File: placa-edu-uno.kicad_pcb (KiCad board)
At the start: 2 copper layers, 97.1 x 58.9 mm, 70 parts, among them J1 Conn_02x20_Odd_Even_MountingP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, J10 HEADER, J11 HEADER, J12 HEADER, J13 HEADER, J14 HEADER, J15 HEADER, J2 Screw_Terminal_01x02, J3 Screw_Terminal_01x02, J4 Screw_Terminal_01x02, J5 Screw_Terminal_01x02, J6 Conn_02x13_Odd_Even, J7 HEADER, J8 HEADER, J9 HEADER, U1 PCA9685PW_118, U2 MAX98357AETE_T, U3 MAX98357AETE_T, U4 ICS-43434, U5 ICS-43434, U6 LM73605

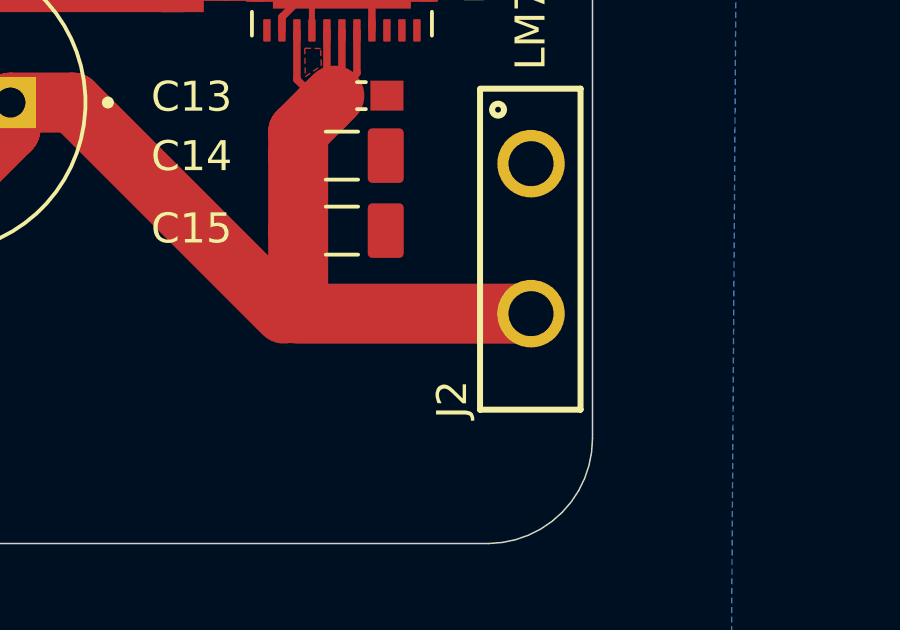
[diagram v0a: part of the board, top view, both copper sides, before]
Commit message: Se agregó símbolo de polaridad a J2 en la serigrafía
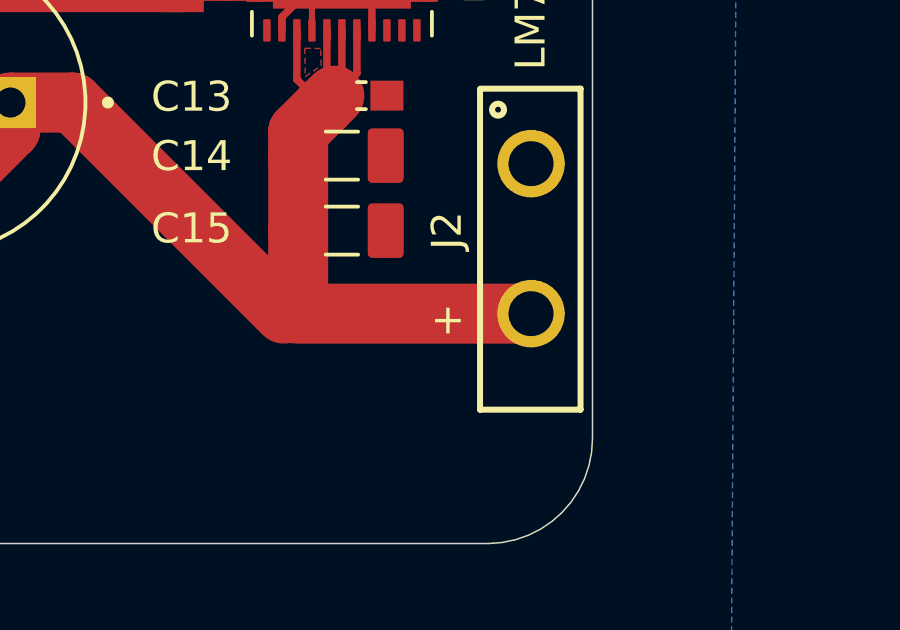
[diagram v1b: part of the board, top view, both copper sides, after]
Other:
- board text added: "+"
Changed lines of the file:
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@@
 		(at 82.804 46.268 -90)
 		(property "Reference" "J2"
-			(at 5.357 2.629 90)
+			(at -0.268 2.804 90)
 			(layer "F.SilkS")
 			(effects
@@
 		(layer "Edge.Cuts")
 	)
+	(gr_text "+"
+		(at 80 49 90)
+		(layer "F.SilkS")
+		(effects
+			(font
+				(size 1 1)
+				(thickness 0.16)
+			)
+		)
+	)
 	(dimension

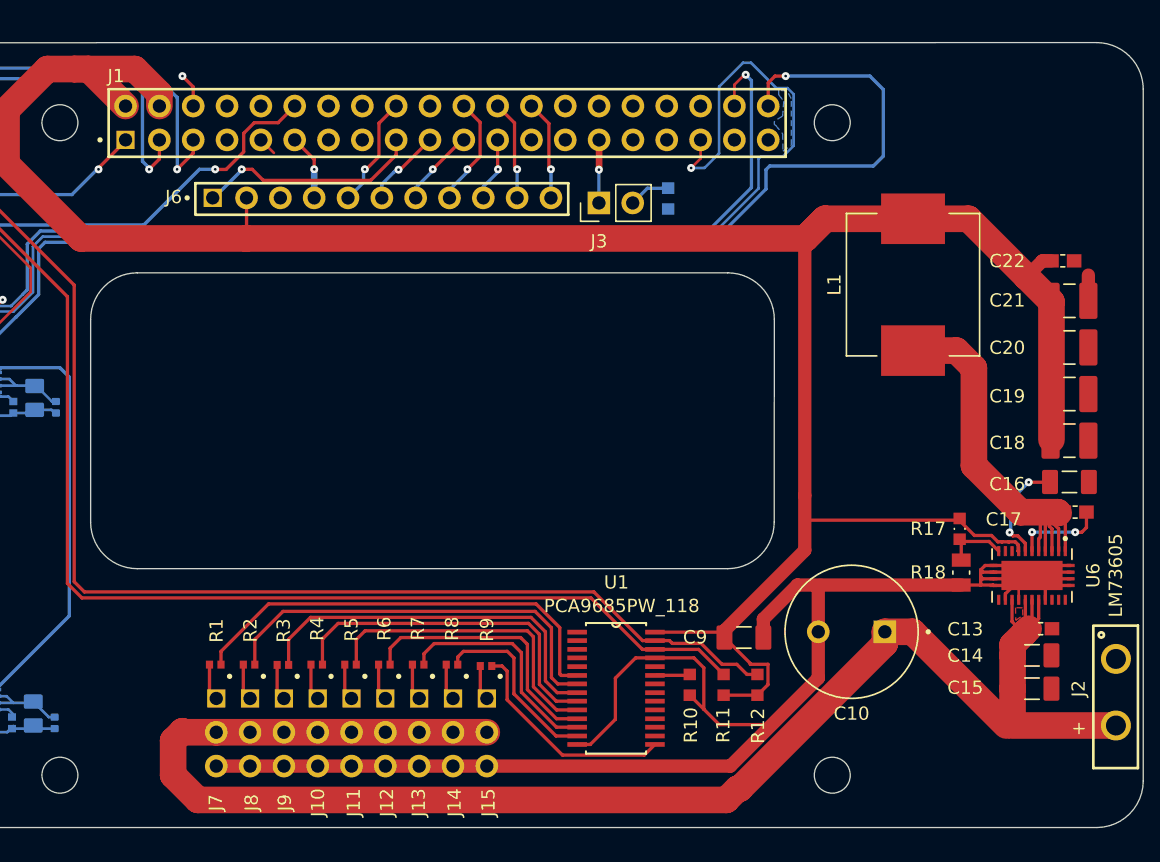
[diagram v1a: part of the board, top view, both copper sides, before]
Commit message: Se añadió serigrafía con nombres, logos y pines de los servos
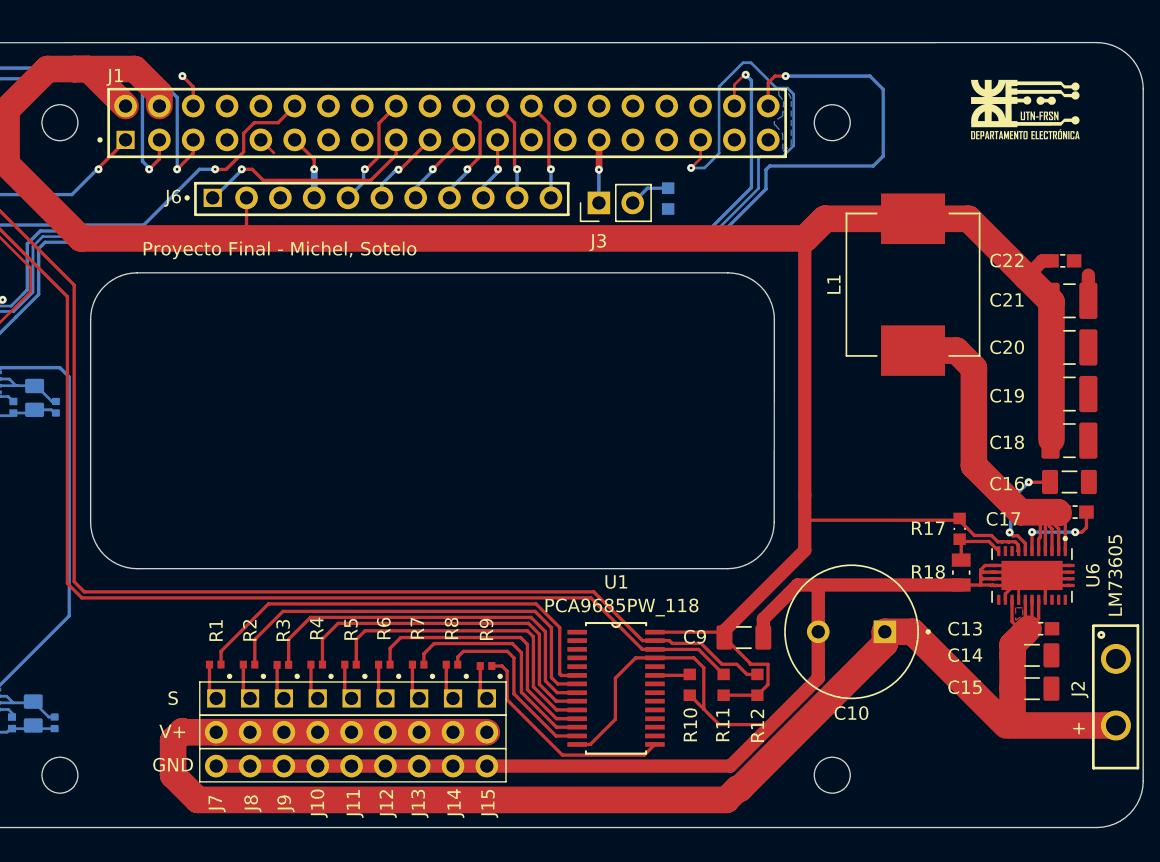
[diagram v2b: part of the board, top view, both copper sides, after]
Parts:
- added G***: LOGO, Footprints:logo_utn, F.Cu at (76.0, 2.50)
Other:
- board text added: "GND"
- board text added: "Proyecto Final - Michel, Sotelo"
- board text added: "S"
- board text added: "V+"

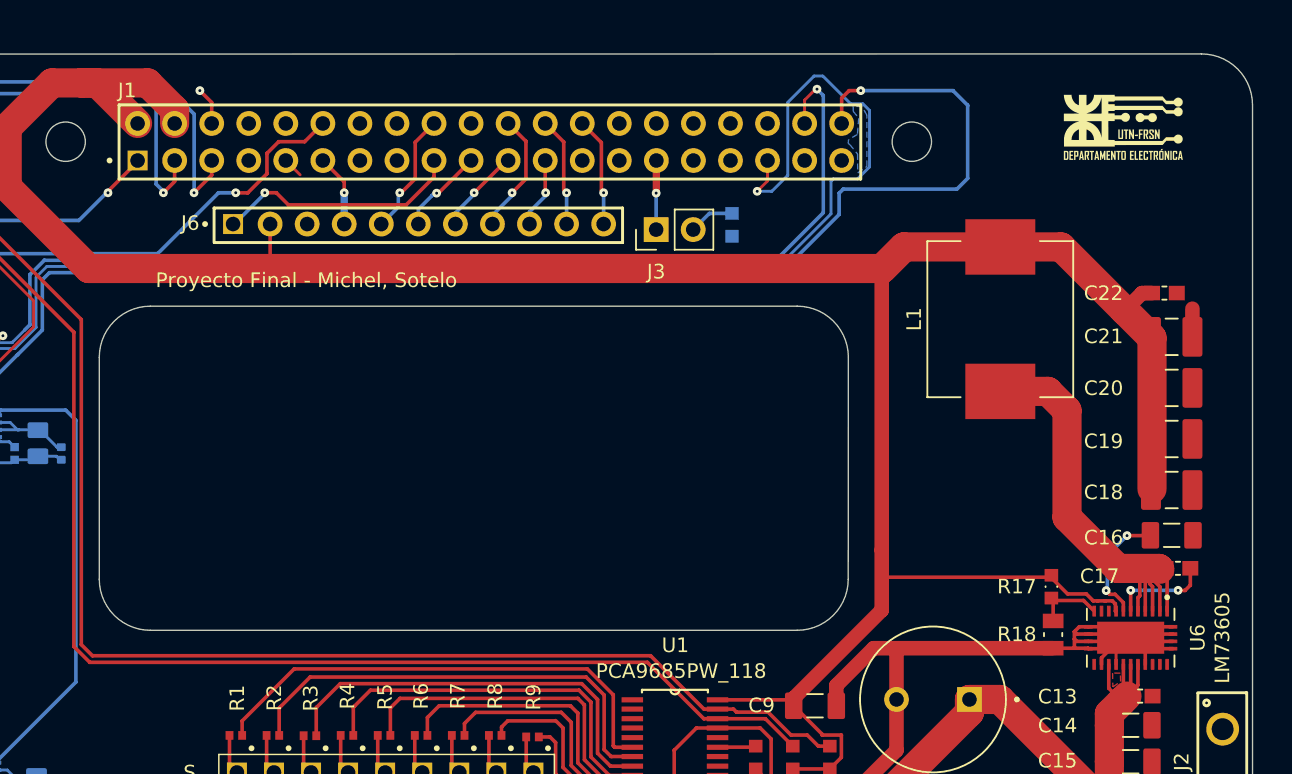
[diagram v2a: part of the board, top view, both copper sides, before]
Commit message: Se corrigio la posicion de la serigrafia en J4 y J5, y el nombre de la U1 PCA9685
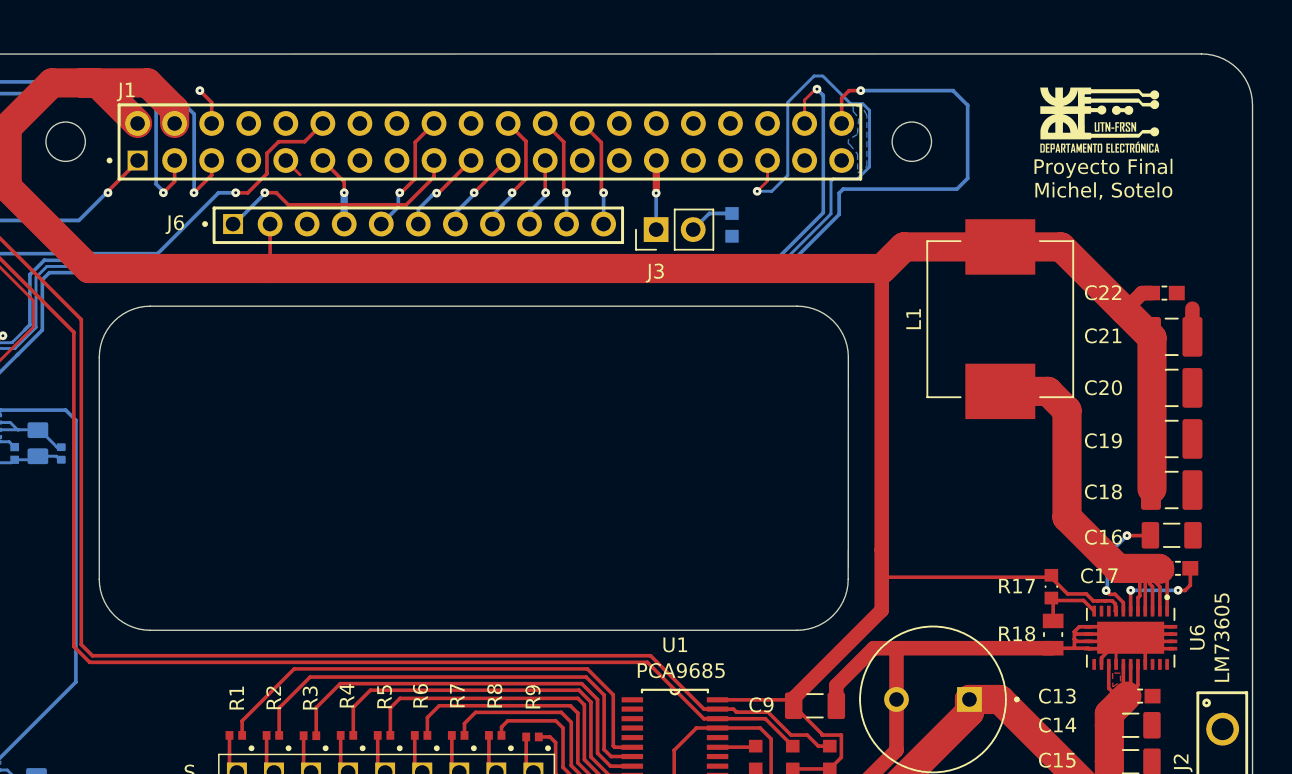
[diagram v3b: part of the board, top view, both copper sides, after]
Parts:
- U1: value PCA9685PW_118 -> PCA9685
- moved G*** 1.69 mm to (74.4, 2.00)
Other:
- board text added: "Proyecto Final Michel, Sotelo"
- board text removed: "Proyecto Final - Michel, Sotelo"
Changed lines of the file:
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@@
 		(at 14.97464 9.144)
 		(property "Reference" "J6"
-			(at -2.93464 -0.064 0)
+			(at -3.91464 -0.054 0)
 			(layer "F.SilkS")
 			(effects
@@
 	(footprint "Footprints:logo_utn"
 		(layer "F.Cu")
-		(at 76 2.5)
+		(at 74.382936 2.002394)
 		(property "Reference" "G***"
 			(at 7.5 -1 0)
@@
 			)
 		)
-		(property "Value" "PCA9685PW_118"
+		(property "Value" "PCA9685"
 			(at 0.4272 -6.184 0)
 			(layer "F.SilkS")
@@
 		(at -10.01 41.78)
 		(property "Reference" "J5"
-			(at 0 0.5 180)
+			(at 0 0.5 0)
 			(unlocked yes)
 			(layer "B.SilkS")
@@
 		(at -9.95 17.13)
 		(property "Reference" "J4"
-			(at 0 0.5 180)
+			(at 0 0.5 0)
 			(unlocked yes)
 			(layer "B.SilkS")
@@
 		)
 	)
-	(gr_text "Proyecto Final - Michel, Sotelo"
-		(at 20 13 0)
+	(gr_text "Proyecto Final\nMichel, Sotelo"
+		(at 74.632936 6.052394 0)
 		(layer "F.SilkS")
 		(effects
@@
 		)
 	)
+	(gr_text "+"
+		(at -10.05 25.12 90)
+		(layer "B.SilkS")
+		(effects
+			(font
+				(size 1 1)
+				(thickness 0.16)
+			)
+		)
+	)
+	(gr_text "+"
+		(at -10.05 49.66 90)
+		(layer "B.SilkS")
+		(effects
+			(font
+				(size 1 1)
+				(thickness 0.125)
+			)
+		)
+	)
 	(dimension
 		(type aligned)
@@
 	)
 	(group ""
+		(members "24964b83-0313-41aa-acba-c239b679768d" "a6e9302c-9ada-484b-ab14-5500d311d555")
+	)
+	(group ""

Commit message: Mejora de ruteo
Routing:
- net GND: track 183.8 -> 145.2 mm
- net 5V_Fuente: track 124.3 -> 103.1 mm
- net GPIO_19_FS_PCM: track 139.0 -> 121.1 mm
- net GPIO_18_CLK_PCM: track 92.6 -> 94.3 mm
- net 3.3V_RPI: track 125.5 -> 126.6 mm
- net GPIO_20_DIN_PCM: track 114.9 -> 115.5 mm
- net GPIO_21_DOUT_PCM: track 125.5 -> 126.1 mm
- net /Amplificadores/OUT_N2: track 4.89 -> 5.43 mm
- added copper zone on F.Cu, net 5V_Fuente

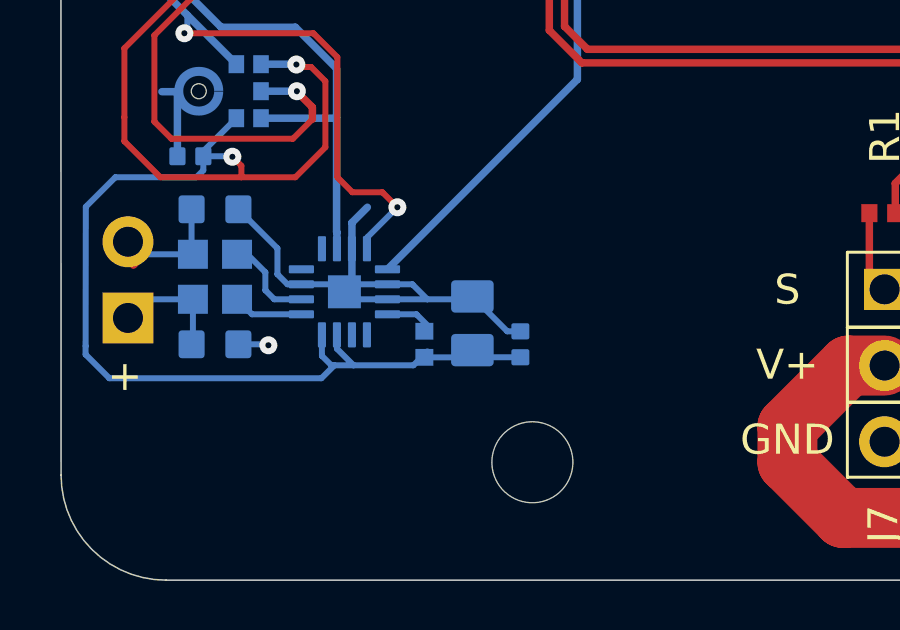
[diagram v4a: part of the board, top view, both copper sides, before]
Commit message: Se movio la posicion de c y r en el amplificador de abajo para que no quede sobre el borde del mounting hole.
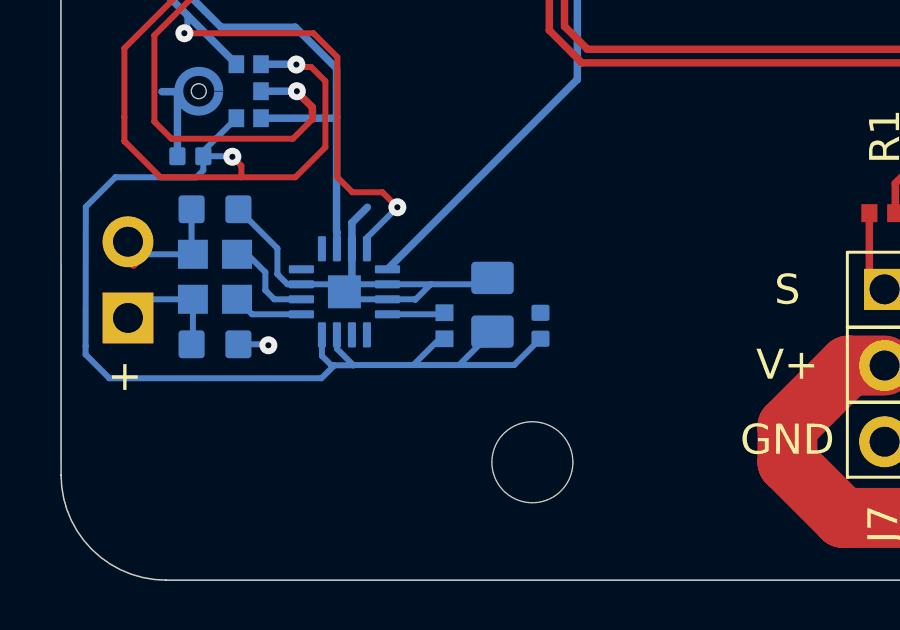
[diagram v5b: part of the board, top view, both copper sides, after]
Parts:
- moved C6 0.91 mm to (2.17, 47.2)
- moved C5 0.91 mm to (3.77, 48.0)
- moved R14 0.91 mm to (0.57, 48.0)
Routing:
- net 3.3V_RPI: track 126.6 -> 130.1 mm
- net GND: track 145.2 -> 143.8 mm
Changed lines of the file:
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@@
 	(footprint "CL21A106KOQNNNE:CAPC2012X140N"
 		(layer "B.Cu")
-		(at 1.5 47.868 90)
+		(at 2.17 47.25 90)
 		(property "Reference" "C6"
 			(at 2.748 0.33 90)
@@
 	(footprint "0402WGF6803TCE:RESC1005X40N"
 		(layer "B.Cu")
-		(at -0.1 48.568 90)
+		(at 0.57 47.95 90)
 		(property "Reference" "R14"
-			(at -2.482 0.12 270)
+			(at 2.99 -0.01 270)
 			(layer "B.SilkS")
 			(effects
@@
 	(footprint "CL05B104KO5NNNC:CAPC1005X55N"
 		(layer "B.Cu")
-		(at 3.1 48.568 90)
+		(at 3.77 47.95 90)
 		(property "Reference" "C5"
 			(at 2.028 0.18 90)
@@
 	)
 	(segment
-		(start 1.405 47.068)
-		(end 1.5 46.973)
-		(width 0.2)
-		(layer "B.Cu")
-		(net 1)
-	)
-	(segment
 		(start -4.2 46.568)
 		(end -3.015 46.568)
@@
 	)
 	(segment
-		(start -0.5 46.568)
-		(end 0 47.068)
+		(start -2.963745 22.747745)
+		(end -2.713745 22.997745)
 		(width 0.2)
 		(layer "B.Cu")
@@
 	)
 	(segment
-		(start -2.963745 22.747745)
-		(end -2.713745 22.997745)
+		(start -1.33 46.568)
+		(end 0.12 46.568)
 		(width 0.2)
 		(layer "B.Cu")
@@
 	)
 	(segment
-		(start 2.663 48.136)
-		(end 1.5 46.973)
-		(width 0.2)
-		(layer "B.Cu")
-		(net 1)
-	)
-	(segment
 		(start -2.515 46.568)
 		(end -2.765 46.818)
@@
 	)
 	(segment
-		(start 1.5 46.973)
-		(end 1.373 47.1)
-		(width 0.2)
-		(layer "B.Cu")
-		(net 1)
-	)
-	(segment
 		(start 60.45 38.36831)
 		(end 60.6 38.21831)
@@
 	)
 	(segment
-		(start 0 47.068)
-		(end 1.405 47.068)
-		(width 0.2)
-		(layer "B.Cu")
-		(net 1)
-	)
-	(segment
-		(start -1.33 47.068)
-		(end 0 47.068)
-		(width 0.2)
-		(layer "B.Cu")
-		(net 1)
-	)
-	(segment
 		(start -8.332 42.3)
 		(end -8.332 40.1895)
@@
 	)
 	(segment
-		(start 3.1 48.136)
-		(end 2.663 48.136)
+		(start 1.957 46.568)
+		(end 2.17 46.355)
+		(width 0.2)
+		(layer "B.Cu")
+		(net 1)
+	)
+	(segment
+		(start 0.112 46.568)
+		(end 0.12 46.568)
 		(width 0.2)
 		(layer "B.Cu")
@@
 	)
 	(segment
-		(start -1.33 46.568)
-		(end -0.5 46.568)
-		(width 0.2)
-		(layer "B.Cu")
-		(net 1)
-	)
-	(segment
 		(start -1.278745 22.747745)
 		(end -0.3 22.747745)
@@
 	)
 	(segment
+		(start -0.4 47.08)
+		(end 0.112 46.568)
+		(width 0.2)
+		(layer "B.Cu")
+		(net 1)
+	)
+	(segment
 		(start -8.332 40.1895)
 		(end -8.29 40.1475)
@@
 	)
 	(segment
+		(start 0.12 46.568)
+		(end 1.957 46.568)
+		(width 0.2)
+		(layer "B.Cu")
+		(net 1)
+	)
+	(segment
 		(start -6.217866 19.317866)
 		(end -6.2 19.3)
@@
 	)
 	(segment
+		(start -1.33 47.068)
+		(end -0.412 47.068)
+		(width 0.2)
+		(layer "B.Cu")
+		(net 1)
+	)
+	(segment
 		(start -5.1 20.336)
 		(end -6.217866 20.336)
@@
 	)
 	(segment
+		(start -0.412 47.068)
+		(end -0.4 47.08)
+		(width 0.2)
+		(layer "B.Cu")
+		(net 1)
+	)
+	(segment
 		(start -6.3 48.568)
 		(end -5.332 48.568)
@@
 	)
 	(segment
-		(start -0.1 49.003)
-		(end 1.26 49.003)
-		(width 0.2)
-		(layer "B.Cu")
-		(net 2)
-	)
-	(segment
 		(start -10.6 49.7)
 		(end -3.532 49.7)
@@
 	)
 	(segment
-		(start -0.465 49.268)
-		(end 0 48.803)
-		(width 0.2)
-		(layer "B.Cu")
-		(net 2)
-	)
-	(segment
 		(start -2.5 25.504)
 		(end -3.1 25.504)
@@
 	(segment
 		(start -2.461842 49.268)
-		(end -0.465 49.268)
-		(width 0.2)
-		(layer "B.Cu")
-		(net 2)
-	)
-	(segment
-		(start 1.26 49.003)
-		(end 1.5 48.763)
+		(end -2.453842 49.26)
 		(width 0.2)
 		(layer "B.Cu")
@@
 	)
 	(segment
-		(start 3.1 49)
-		(end 1.737 49)
+		(start 1.055 49.26)
+		(end 2.13745 48.17755)
+		(width 0.2)
+		(layer "B.Cu")
+		(net 2)
+	)
+	(segment
+		(start -2.453842 49.26)
+		(end -0.473 49.26)
 		(width 0.2)
 		(layer "B.Cu")
@@
 	)
 	(segment
+		(start 0.4065 48.385)
+		(end 0.57 48.385)
+		(width 0.2)
+		(layer "B.Cu")
+		(net 2)
+	)
+	(segment
 		(start -4.376884 39.232)
 		(end -4.366942 39.241942)
@@
 	)
 	(segment
-		(start 1.737 49)
-		(end 1.5 48.763)
-		(width 0.2)
-		(layer "B.Cu")
-		(net 2)
-	)
-	(segment
 		(start -2.5 25.504)
 		(end -0.201 25.504)
@@
 	)
 	(segment
+		(start -0.465 49.2565)
+		(end 0.4065 48.385)
+		(width 0.2)
+		(layer "B.Cu")
+		(net 2)
+	)
+	(segment
 		(start -3.532 49.7)
 		(end -3.1 49.268)
@@
 	)
 	(segment
+		(start 2.892 49.26)
+		(end 3.77 48.382)
+		(width 0.2)
+		(layer "B.Cu")
+		(net 2)
+	)
+	(segment
 		(start -7.468 42.3)
 		(end -6.51645 42.3)
@@
 	)
 	(segment
+		(start 1.055 49.26)
+		(end 2.892 49.26)
+		(width 0.2)
+		(layer "B.Cu")
+		(net 2)
+	)
+	(segment
 		(start 1.6 25.063)
 		(end 2.865416 25.063)
@@
 	)
 	(segment
+		(start -0.473 49.26)
+		(end 1.055 49.26)
+		(width 0.2)
+		(layer "B.Cu")
+		(net 2)
+	)
+	(segment
 		(start -0.201 25.504)
 		(end 0 25.303)
@@
 	)
 	(segment
-		(start -0.365 47.568)
-		(end 0 47.933)
+		(start -1.33 47.568)
+		(end 0.517 47.568)
 		(width 0.2)
 		(layer "B.Cu")
@@
 	)
 	(segment
-		(start -1.33 47.568)
-		(end -0.365 47.568)
+		(start 0.517 47.568)
+		(end 0.57 47.515)
 		(width 0.2)
 		(layer "B.Cu")
